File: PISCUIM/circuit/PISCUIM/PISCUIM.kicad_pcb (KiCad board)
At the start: 2 copper layers, 73 parts, among them CON1 BARREL_JACK, CON10 BARREL_JACK, CON11 BARREL_JACK, CON12 BARREL_JACK, CON13 BARREL_JACK, CON14 BARREL_JACK, CON15 BARREL_JACK, CON16 BARREL_JACK, CON17 BARREL_JACK, CON18 BARREL_JACK, CON19 BARREL_JACK, CON2 BARREL_JACK, CON20 BARREL_JACK, CON3 BARREL_JACK, CON4 BARREL_JACK, CON5 BARREL_JACK, CON6 BARREL_JACK, CON7 BARREL_JACK, CON8 BARREL_JACK, CON9 BARREL_JACK, IC1 PIC16F1938, P1 CONN_01X06, P2 CONN_01X06, P3 CONN_01X06, P4 CONN_01X10, P5 CONN_01X08, P6 CONN_01X08, P7 CONN_01X10, P8 GINGA_voltage_selector, Q1 EKI04047, Q10 EKI04047, Q11 EKI04047, Q12 EKI04047, Q13 EKI04047, Q14 EKI04047, Q15 EKI04047, Q16 EKI04047, Q17 EKI04047, Q18 EKI04047, Q19 EKI04047, Q2 EKI04047, Q20 EKI04047, Q3 EKI04047, Q4 EKI04047, Q5 EKI04047, Q6 EKI04047, Q7 EKI04047, Q8 EKI04047, Q9 EKI04047

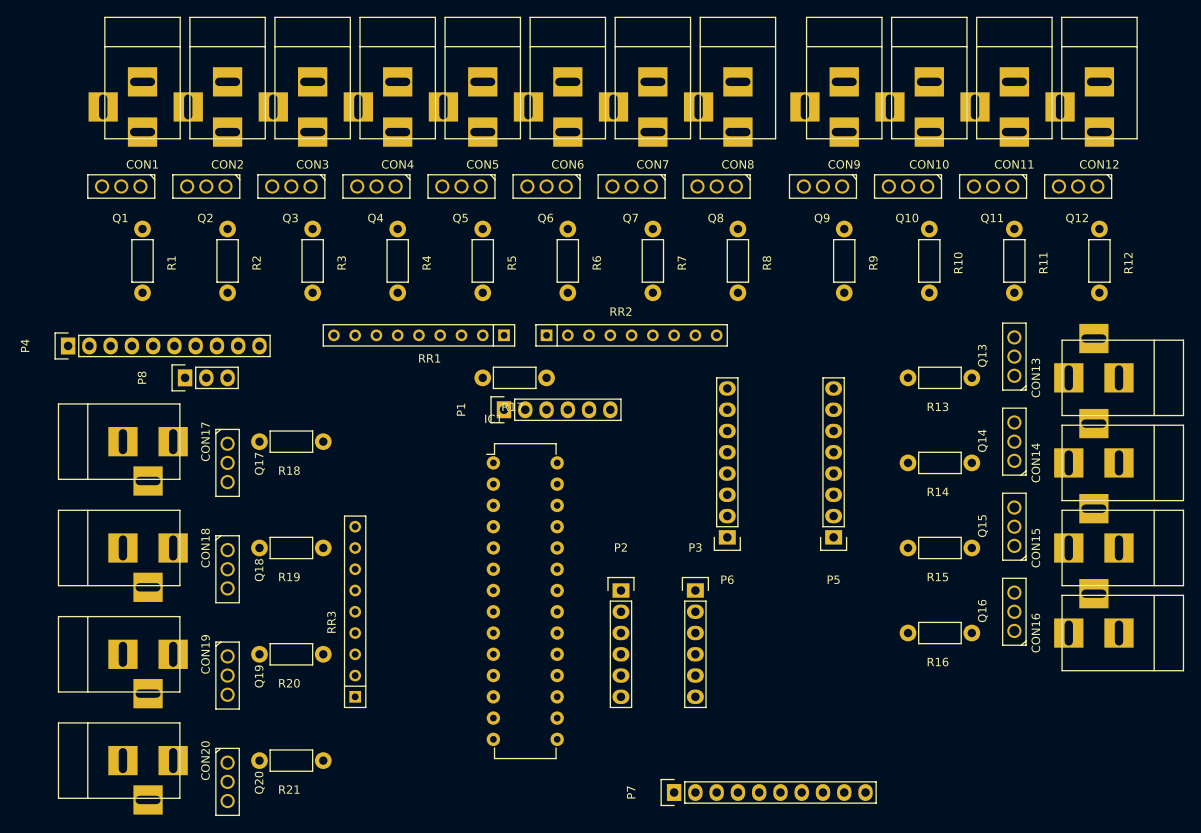
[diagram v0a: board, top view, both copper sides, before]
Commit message: modified circuit diagram and made little changes in code(unfinished)
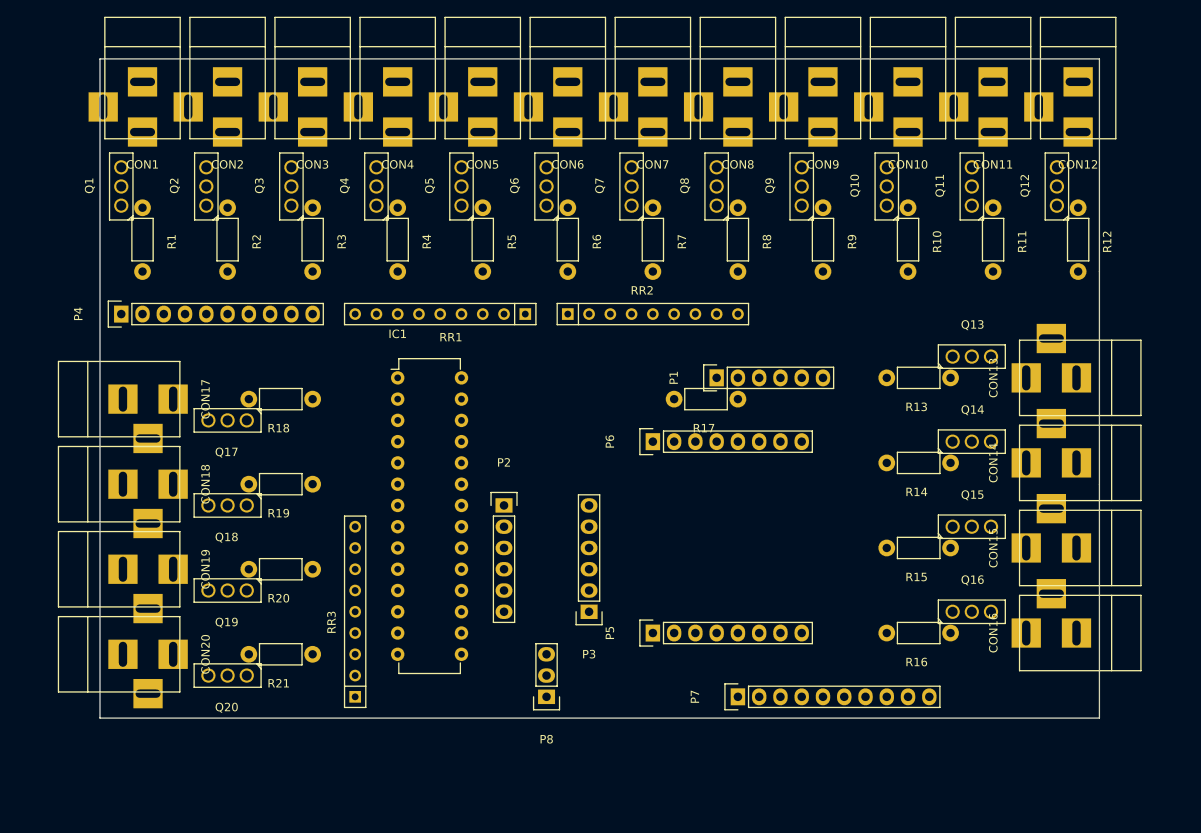
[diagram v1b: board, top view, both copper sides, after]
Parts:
- moved P8 57.6 mm to (119.4, 116.8), turned to 180 degrees
- moved P1 25.7 mm to (139.7, 78.7)
- moved P5 24.4 mm to (132.1, 109.2), turned to 90 degrees
- moved R17 23.0 mm to (142.2, 81.3)
- moved P2 17.3 mm to (114.3, 94.0)
- moved IC1 15.3 mm to (101.6, 78.7)
- moved P6 14.5 mm to (132.1, 86.4), turned to 90 degrees
- moved P7 13.7 mm to (142.2, 116.8)
- moved P3 13.0 mm to (124.5, 106.7), turned to 180 degrees
- moved R21 12.8 mm to (91.4, 111.8)
- moved Q20 12.7 mm to (81.3, 114.3), turned to 180 degrees
- moved CON20 12.7 mm to (68.6, 111.8)
- moved R20 10.2 mm to (91.4, 101.6)
- moved CON19 10.2 mm to (68.6, 101.6)
- moved Q19 10.2 mm to (81.3, 104.1), turned to 180 degrees
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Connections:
- P4 pad 7: 5V_GINGA -> +12V
- P4 pad 8: 12V_GINGA -> +12V
- P6 pad 1: Net-(P6-Pad1) -> Net-(P3-Pad2)
- P6 pad 2: Net-(P6-Pad2) -> Net-(P3-Pad1)
- P6 pad 3: Net-(P3-Pad2) -> Net-(P6-Pad3)
- P6 pad 4: Net-(P3-Pad1) -> Net-(P6-Pad4)
- P7 pad 1: +12V -> 5V_GINGA
- P7 pad 10: 3.3V_LOGIC -> +12V
- P7 pad 2: +12V -> 12V_GINGA
- P7 pad 3: +12V -> 5V_LOGIC
- P7 pad 4: +12V -> 3.3V_LOGIC
- P7 pad 9: 5V_LOGIC -> +12V
- RR3 pad 3: Net-(RR3-Pad3) -> Net-(IC1-Pad14)
- RR3 pad 4: Net-(RR3-Pad4) -> Net-(IC1-Pad13)
- RR3 pad 5: Net-(RR3-Pad5) -> Net-(IC1-Pad12)
- RR3 pad 6: Net-(IC1-Pad14) -> Net-(IC1-Pad11)
- RR3 pad 7: Net-(IC1-Pad13) -> Net-(RR3-Pad7)
- RR3 pad 8: Net-(IC1-Pad12) -> Net-(RR3-Pad8)
- RR3 pad 9: Net-(IC1-Pad11) -> Net-(RR3-Pad9)
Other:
- board outline added: 119.4 x 78.7 mm
- net class universal_board added: clearance 0.2, trace_width 0.6, via_dia 0.6, via_drill 0.4

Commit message: minor change in power line
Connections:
- P7 pad 5: +12V -> 12V_SEIZAE1
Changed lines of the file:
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@@
     (links 156)
     (no_connects 156)
-    (area 60.804379 35.404379 190.655621 123.015)
+    (area 65.964999 40.564999 185.495001 119.455001)
     (thickness 1.6)
     (drawings 6)
@@
       (net 78 3.3V_LOGIC))
     (pad 5 thru_hole oval (at 0 10.16 90) (size 2.032 1.7272) (drill 1.016) (layers *.Cu *.Mask F.SilkS)
-      (net 53 +12V))
+      (net 1 12V_SEIZAE1))
     (pad 6 thru_hole oval (at 0 12.7 90) (size 2.032 1.7272) (drill 1.016) (layers *.Cu *.Mask F.SilkS)
       (net 53 +12V))
